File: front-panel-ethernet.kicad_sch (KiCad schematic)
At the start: 6 parts, among them J3 L834-1G1T-S7

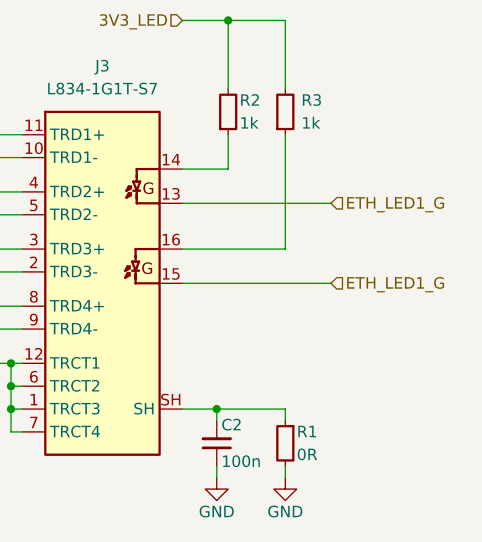
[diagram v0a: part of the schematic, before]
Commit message: [#82153] Fix LED2 label on ETH sheet
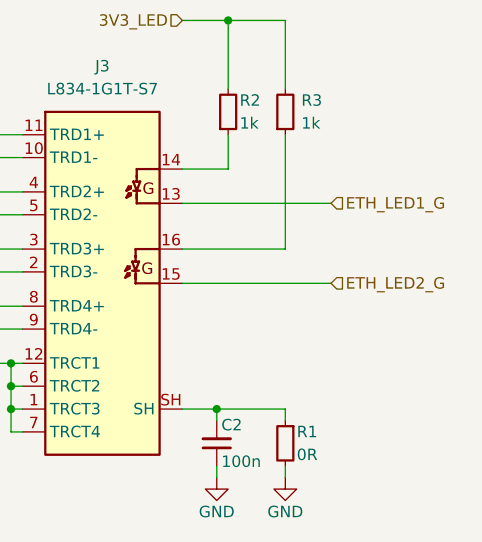
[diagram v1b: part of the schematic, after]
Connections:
- net ETH_LED1_G: no longer J3.15
- new net ETH_LED2_G: J3.15
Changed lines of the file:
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@@
 		)
 	)
-	(hierarchical_label "ETH_LED1_G"
+	(hierarchical_label "ETH_LED2_G"
 		(shape input)
 		(at 222.25 125.73 0)

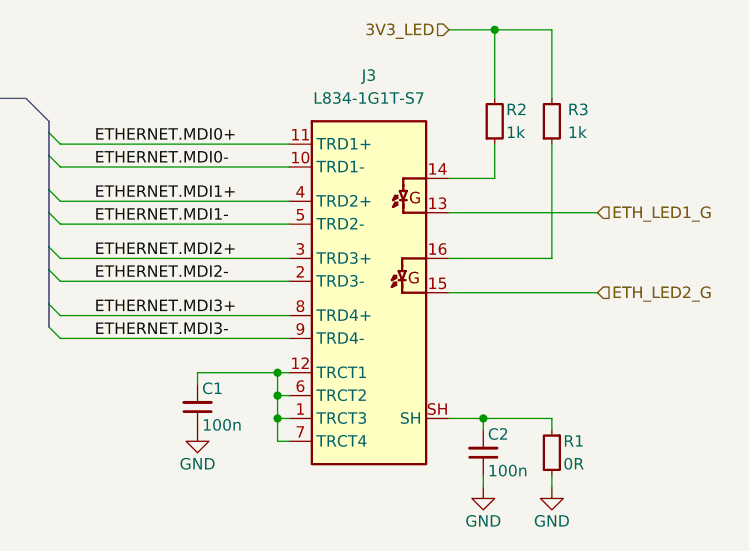
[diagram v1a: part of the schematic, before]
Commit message: [#82176] Fix conflicting annotations
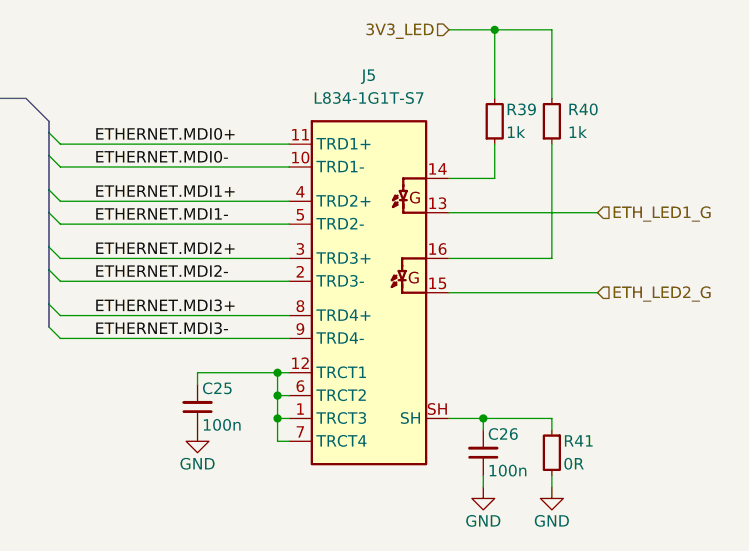
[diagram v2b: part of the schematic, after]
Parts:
- renumbered C1 to C25, C2 to C26, J3 to J5, R2 to R39, R3 to R40, R1 to R41
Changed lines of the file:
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@@
 		(on_board yes)
 		(dnp no)
-		(property "Reference" "#PWR012"
+		(property "Reference" "#PWR053"
 			(at 226.06 149.86 0)
 			(effects
@@
 			(project "bmc-reference-carrier-board"
 				(path "/5f636c45-3c15-4731-8931-4625e0dab7e4/9da0fa42-de01-45ef-a25f-792bb7803b7a"
-					(reference "#PWR012")
+					(reference "#PWR053")
 					(unit 1)
 				)
@@
 		(on_board yes)
 		(dnp no)
-		(property "Reference" "#PWR03"
+		(property "Reference" "#PWR052"
 			(at 218.44 149.86 0)
 			(effects
@@
 			(project "bmc-reference-carrier-board"
 				(path "/5f636c45-3c15-4731-8931-4625e0dab7e4/9da0fa42-de01-45ef-a25f-792bb7803b7a"
-					(reference "#PWR03")
+					(reference "#PWR052")
 					(unit 1)
 				)
@@
 		(on_board yes)
 		(dnp no)
-		(property "Reference" "C2"
+		(property "Reference" "C26"
 			(at 210.058 141.478 90)
 			(effects
@@
 			(project "bmc-reference-carrier-board"
 				(path "/5f636c45-3c15-4731-8931-4625e0dab7e4/9da0fa42-de01-45ef-a25f-792bb7803b7a"
-					(reference "C2")
+					(reference "C26")
 					(unit 1)
 				)
@@
 		(on_board yes)
 		(dnp no)
-		(property "Reference" "#PWR02"
+		(property "Reference" "#PWR051"
 			(at 186.69 143.51 0)
 			(effects
@@
 			(project ""
 				(path "/5f636c45-3c15-4731-8931-4625e0dab7e4/9da0fa42-de01-45ef-a25f-792bb7803b7a"
-					(reference "#PWR02")
+					(reference "#PWR051")
 					(unit 1)
 				)
@@
 		(on_board yes)
 		(dnp no)
-		(property "Reference" "R1"
+		(property "Reference" "R41"
 			(at 218.44 142.24 90)
 			(effects
@@
 			(project ""
 				(path "/5f636c45-3c15-4731-8931-4625e0dab7e4/9da0fa42-de01-45ef-a25f-792bb7803b7a"
-					(reference "R1")
+					(reference "R41")
 					(unit 1)
 				)
@@
 		(on_board yes)
 		(dnp no)
-		(property "Reference" "R2"
+		(property "Reference" "R39"
 			(at 212.09 105.41 90)
 			(effects
@@
 			(project ""
 				(path "/5f636c45-3c15-4731-8931-4625e0dab7e4/9da0fa42-de01-45ef-a25f-792bb7803b7a"
-					(reference "R2")
+					(reference "R39")
 					(unit 1)
 				)
@@
 		(on_board yes)
 		(dnp no)
-		(property "Reference" "C1"
+		(property "Reference" "C25"
 			(at 178.308 136.398 90)
 			(effects
@@
 			(project ""
 				(path "/5f636c45-3c15-4731-8931-4625e0dab7e4/9da0fa42-de01-45ef-a25f-792bb7803b7a"
-					(reference "C1")
+					(reference "C25")
 					(unit 1)
 				)
@@
 		(on_board yes)
 		(dnp no)
-		(property "Reference" "R3"
+		(property "Reference" "R40"
 			(at 218.948 105.41 90)
 			(effects
@@
 			(project "bmc-reference-carrier-board"
 				(path "/5f636c45-3c15-4731-8931-4625e0dab7e4/9da0fa42-de01-45ef-a25f-792bb7803b7a"
-					(reference "R3")
+					(reference "R40")
 					(unit 1)
 				)
@@
 		(dnp no)
 		(fields_autoplaced yes)
-		(property "Reference" "J3"
+		(property "Reference" "J5"
 			(at 196.85 101.6 0)
 			(effects
@@
 			(project ""
 				(path "/5f636c45-3c15-4731-8931-4625e0dab7e4/9da0fa42-de01-45ef-a25f-792bb7803b7a"
-					(reference "J3")
+					(reference "J5")
 					(unit 1)
 				)

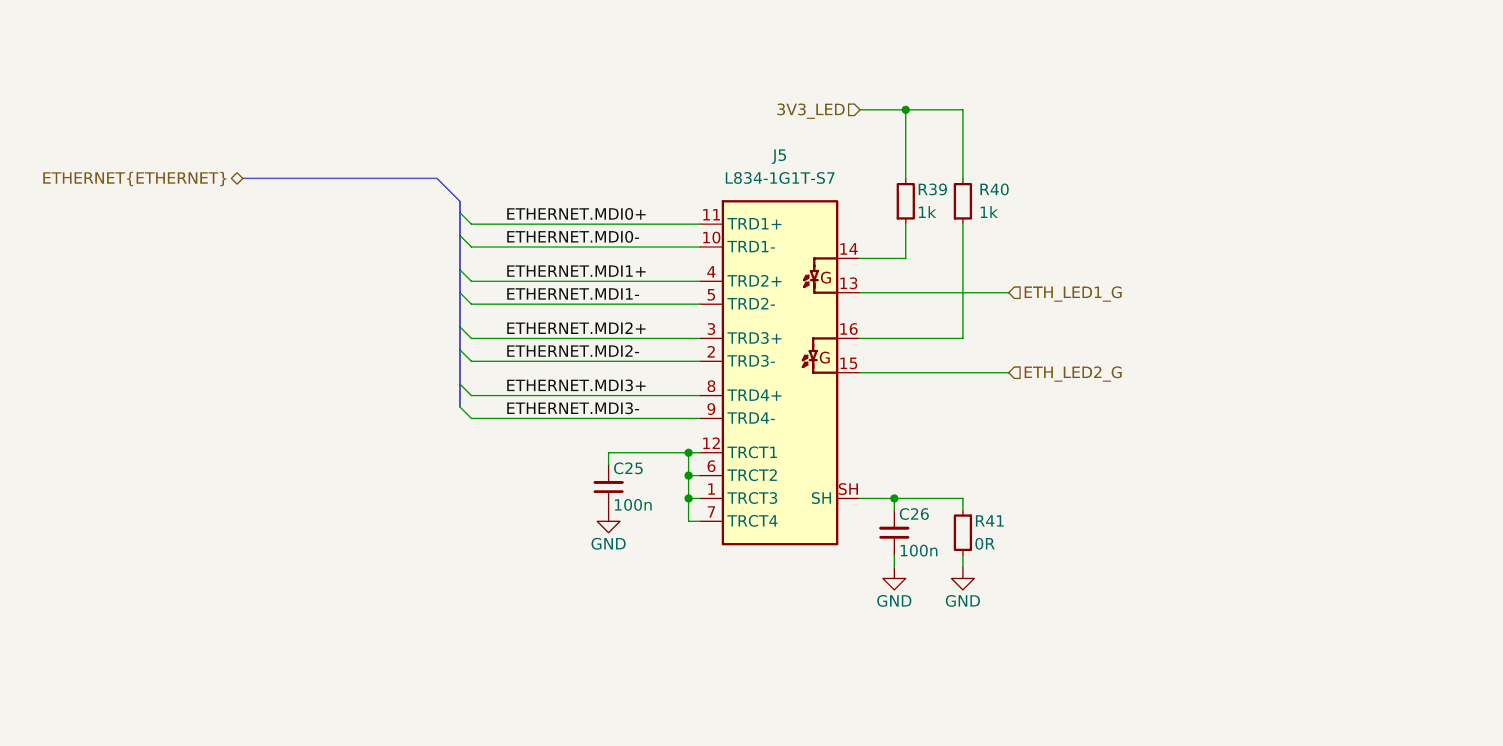
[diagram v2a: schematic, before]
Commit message: Replace Eth connector with 7498111120R
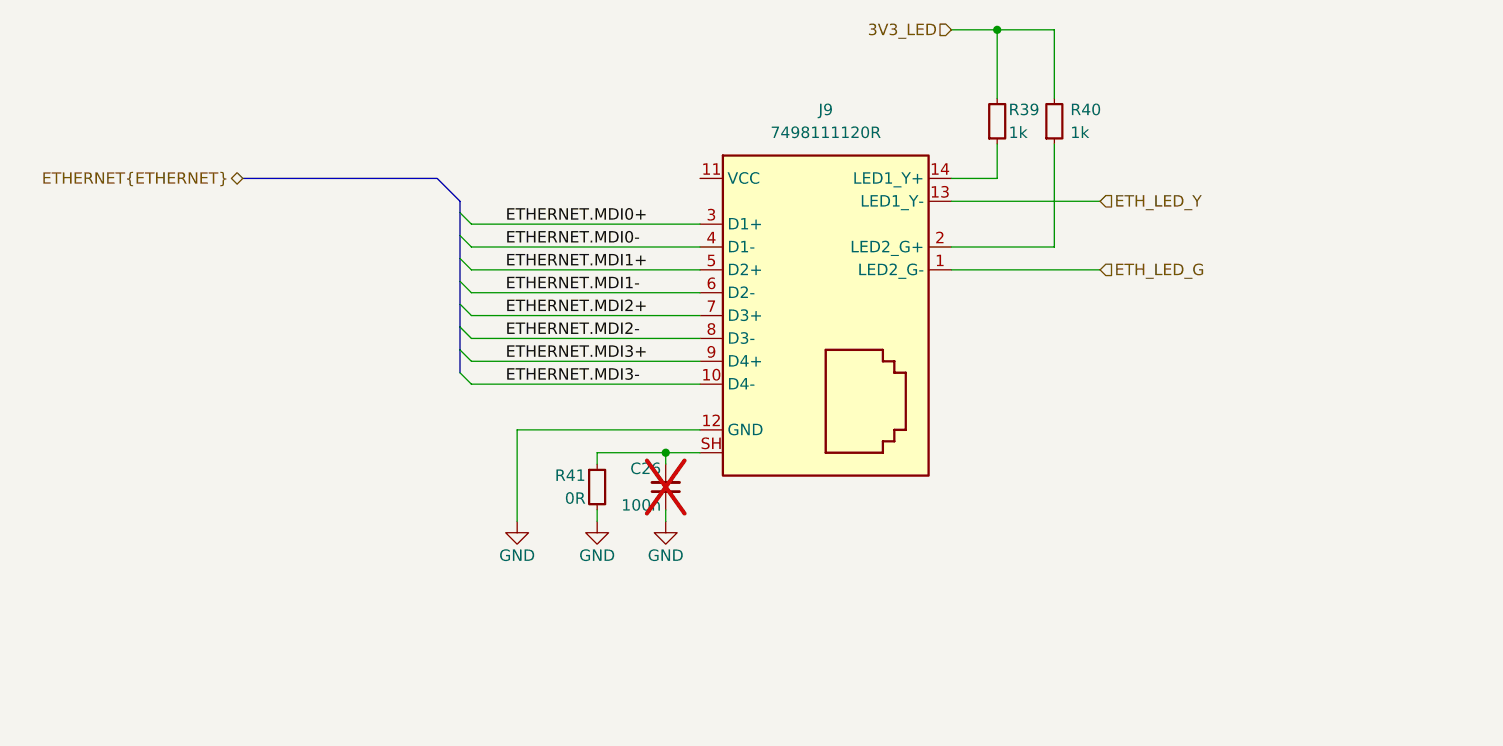
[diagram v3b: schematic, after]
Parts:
- removed C25: C_100n_0402, antmicro-footprints:C_0402_1005Metric, symbol antmicroCapacitors0402:C_100n_0402
- removed J5: L834-1G1T-S7, antmicro-footprints:RJ45_BEL_L834-1G1T-S7, symbol antmicroModularConnectorsJacksWithMagnetics:L834-1G1T-S7
- added J9: Bus_RJ45_7498111120R, antmicro-footprints:Bus_RJ45_7498111120R, symbol antmicroModularConnectorsJacksWithMagnetics:Bus_RJ45_7498111120R
- C26: now not fitted; now left out of the parts list
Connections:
- net ETHERNET.MDI0+: now also J9.3 (D1+)
- net ETHERNET.MDI0-: now also J9.4 (D1-)
- net ETHERNET.MDI1+: now also J9.5 (D2+)
- net ETHERNET.MDI1-: now also J9.6 (D2-)
- net ETHERNET.MDI2+: now also J9.7 (D3+)
- net ETHERNET.MDI2-: now also J9.8 (D3-)
- net ETHERNET.MDI3+: now also J9.9 (D4+)
- net ETHERNET.MDI3-: now also J9.10 (D4-)
- net GND: now also J9.12 (GND)
- net at C26.2, R41.1: now also J9.SH
- net at R39.1: now also J9.14 (LED1_Y+)
- net at R40.1: now also J9.2 (LED2_G+)
- new net ETH_LED_G: J9.1 (LED2_G-)
- new net ETH_LED_Y: J9.13 (LED1_Y-)
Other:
- moved on the sheet: R39, R40, R41

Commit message: Changed A4 sheets to A3 and cleaned them up
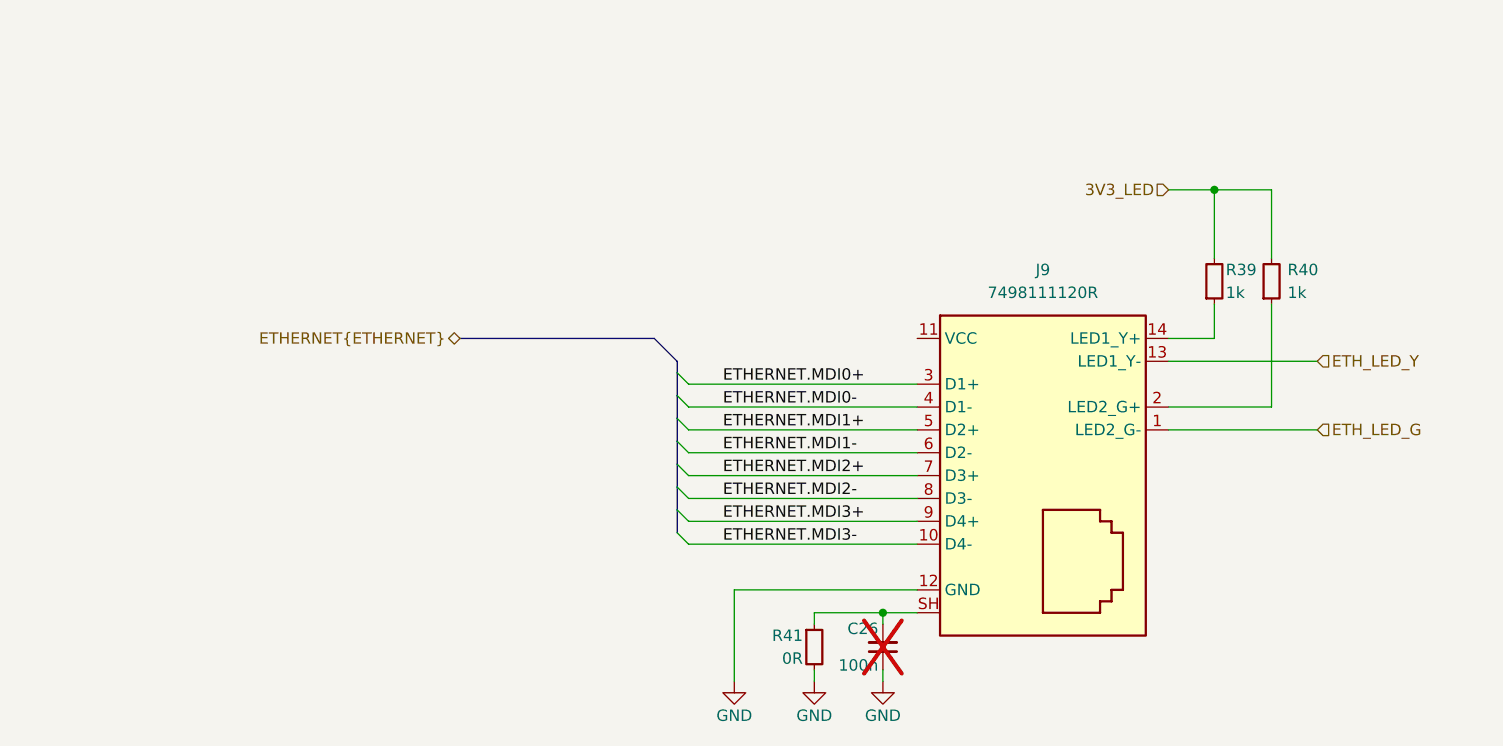
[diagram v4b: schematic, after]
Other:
- moved on the sheet: C26, J9, R39, R40, R41

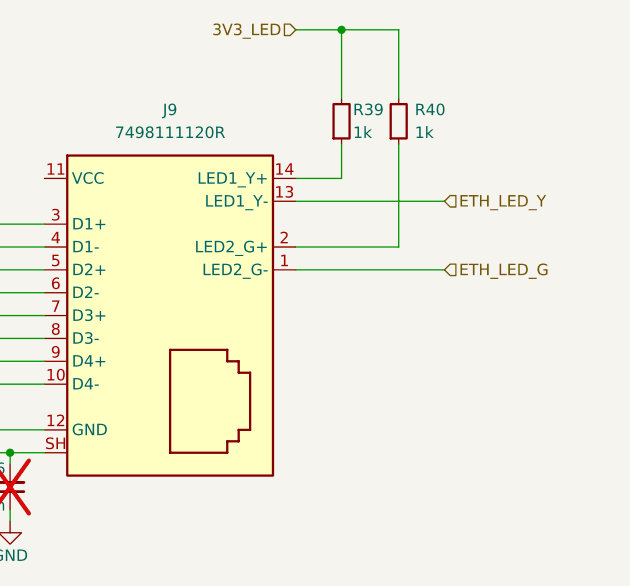
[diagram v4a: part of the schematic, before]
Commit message: [#83329] Finish connecting ETH PHY, connect ETH LEDs, adjust PHY power supply filtering
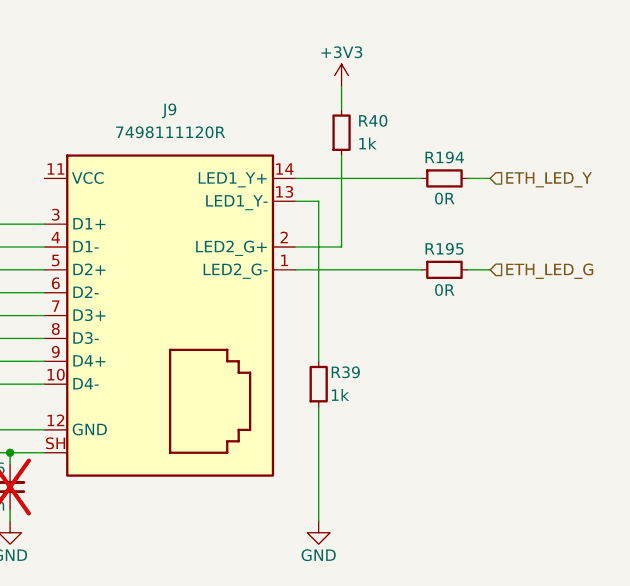
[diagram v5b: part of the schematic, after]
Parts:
- added R194, R195: R_0R_0402, antmicro-footprints:R_0402_1005Metric, symbol antmicroResistors0402:R_0R_0402
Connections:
- net ETH_LED_G: now also R195.2; no longer J9.1 (LED2_G-)
- net ETH_LED_Y: now also R194.2; no longer J9.13 (LED1_Y-)
- net GND: now also R39.1
- net at J9.14 (LED1_Y+): now also R194.1; no longer R39.1
- net 3V3_LED: no longer names the net of R39.2
- net 3V3_LED: now also J9.13 (LED1_Y-); no longer R40.2
- new net: J9.1 (LED2_G-), R195.1
- new net +3V3: R40.2
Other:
- moved on the sheet: R39, R40

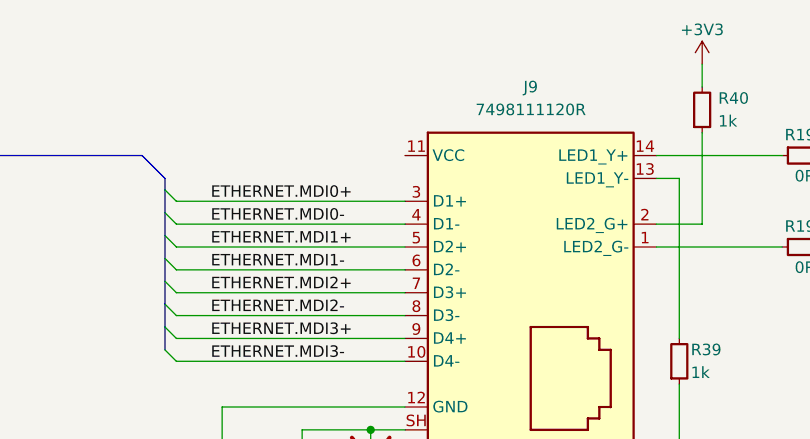
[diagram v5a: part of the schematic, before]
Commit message: [#83329] Small ethernet PHY fixes
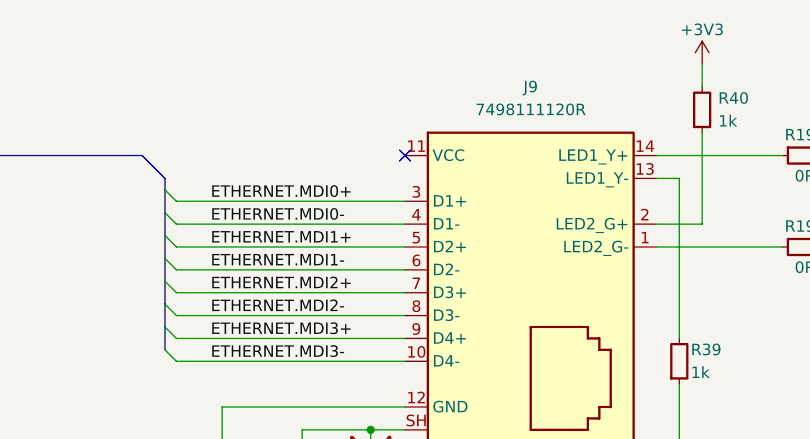
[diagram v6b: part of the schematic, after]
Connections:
- no-connect marks 0 -> 1
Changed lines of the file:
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@@
 		(color 0 0 0 0)
+	)
+	(no_connect
+		(at 212.09 121.92)
 	)
 	(bus_entry

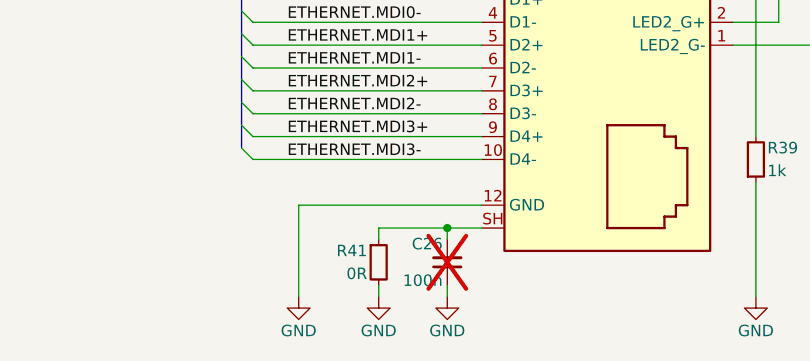
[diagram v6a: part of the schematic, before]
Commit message: [#83336] Small front panel interface fixes
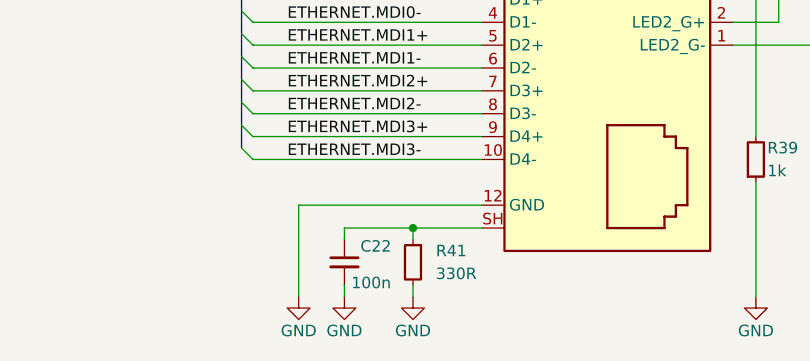
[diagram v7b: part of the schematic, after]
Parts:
- removed C26: C_100n_0402, antmicro-footprints:C_0402_1005Metric, symbol antmicroCapacitors0402:C_100n_0402
- removed R41: R_0R_0402, antmicro-footprints:R_0402_1005Metric, symbol antmicroResistors0402:R_0R_0402
- added C22: C_100n_0402, antmicro-footprints:C_0402_1005Metric, symbol antmicroCapacitors0402:C_100n_0402
- added R41: R_330R_0402, antmicro-footprints:R_0402_1005Metric, symbol antmicroResistors0402:R_330R_0402
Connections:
- net GND: now also C22.2, R41.2
- net at J9.SH: now also C22.1, R41.1
